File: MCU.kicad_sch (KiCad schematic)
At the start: 28 parts, among them U2 STM32H743VIT6, Y1 8MHz

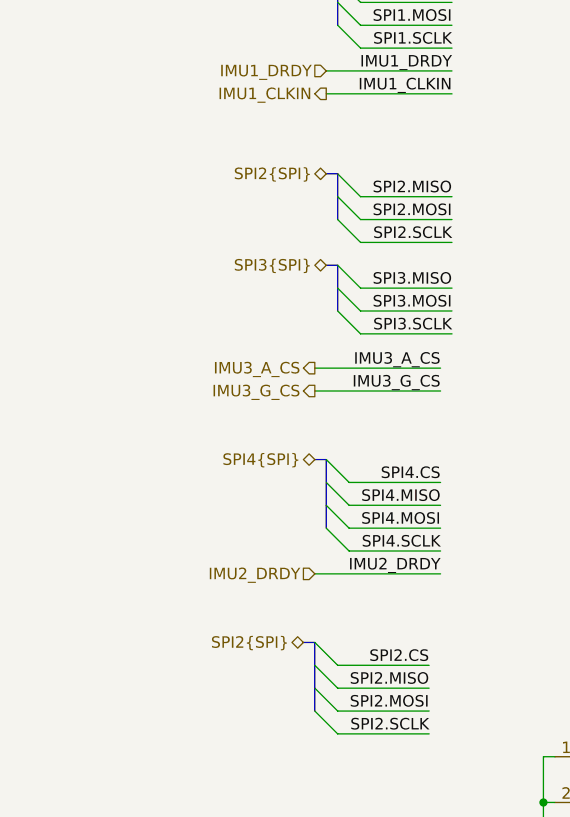
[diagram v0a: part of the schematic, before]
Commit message: Define SPI2 bus members across MCU and sensors
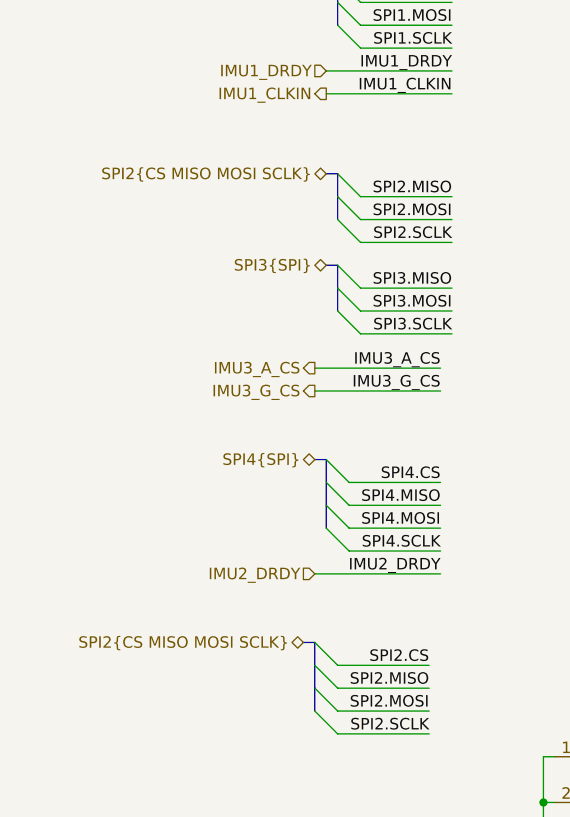
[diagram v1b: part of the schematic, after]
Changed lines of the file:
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@@
 		)
 	)
-	(hierarchical_label "SPI2{SPI}"
+	(hierarchical_label "SPI2{CS MISO MOSI SCLK}"
 		(shape bidirectional)
 		(at 30.48 130.81 180)
@@
 		)
 	)
-	(hierarchical_label "SPI2{SPI}"
+	(hierarchical_label "SPI2{CS MISO MOSI SCLK}"
 		(shape bidirectional)
 		(at 33.02 78.74 180)

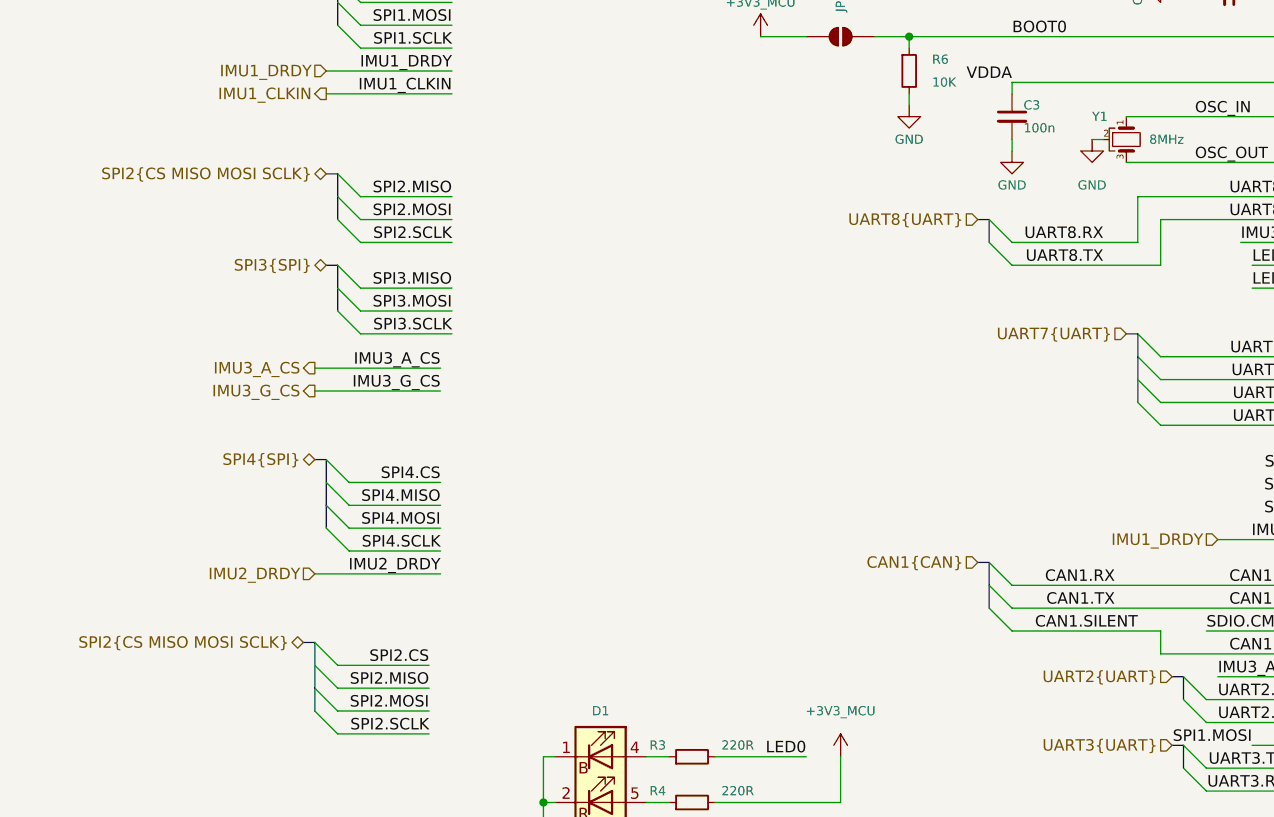
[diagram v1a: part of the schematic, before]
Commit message: Define reusable aliases for hierarchical buses
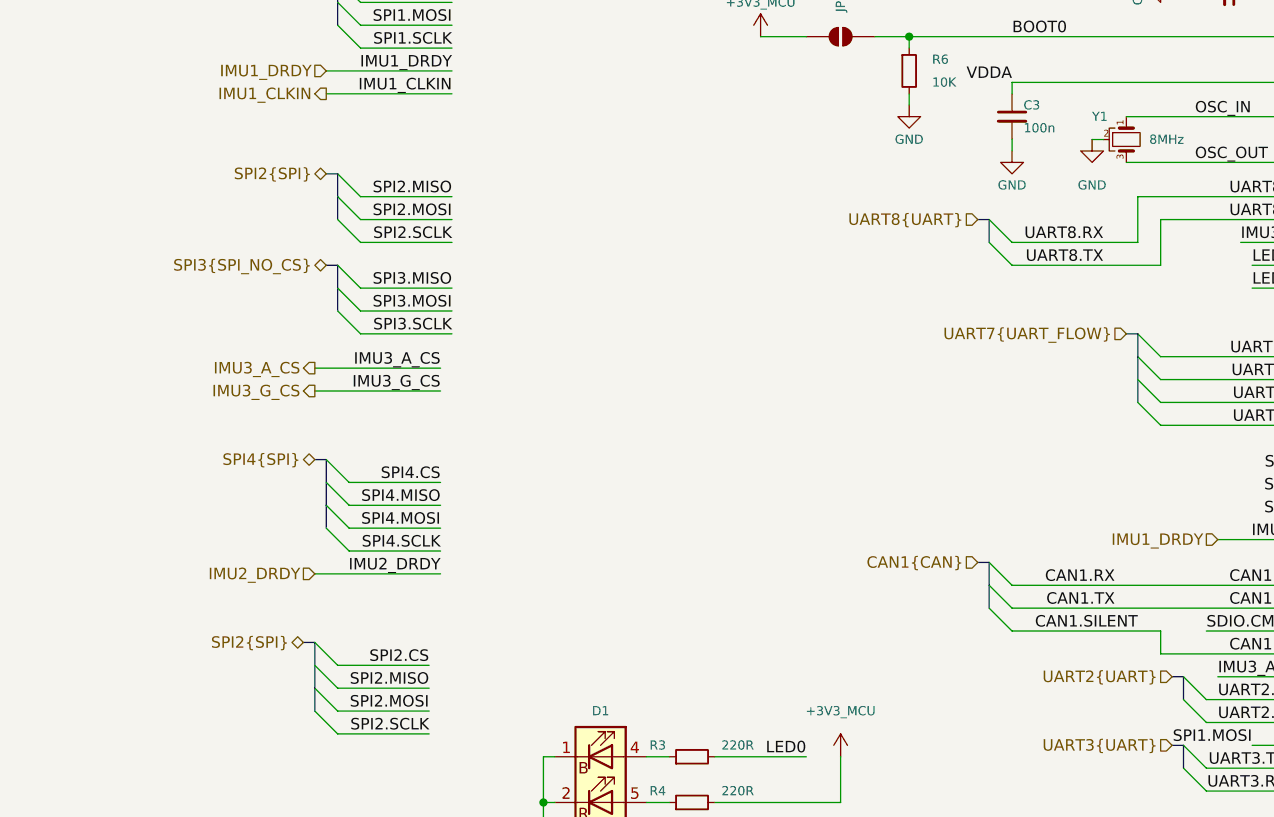
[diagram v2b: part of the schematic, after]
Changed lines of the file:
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@@
 		)
 	)
-	(hierarchical_label "SPI3{SPI}"
+	(hierarchical_label "SPI3{SPI_NO_CS}"
 		(shape bidirectional)
 		(at 33.02 88.9 180)
@@
 		)
 	)
-	(hierarchical_label "SPI2{CS MISO MOSI SCLK}"
+	(hierarchical_label "SPI2{SPI}"
 		(shape bidirectional)
 		(at 30.48 130.81 180)
@@
 		)
 	)
-	(hierarchical_label "SPI2{CS MISO MOSI SCLK}"
+	(hierarchical_label "SPI2{SPI}"
 		(shape bidirectional)
 		(at 33.02 78.74 180)
@@
 		)
 	)
-	(hierarchical_label "UART7{UART}"
+	(hierarchical_label "UART7{UART_FLOW}"
 		(shape input)
 		(at 121.92 96.52 180)

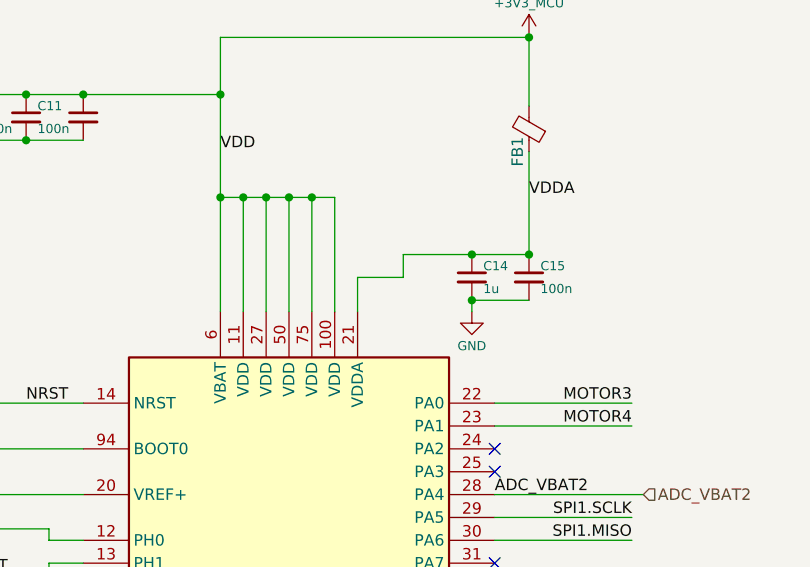
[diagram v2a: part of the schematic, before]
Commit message: Declare external and regulator power sources for ERC
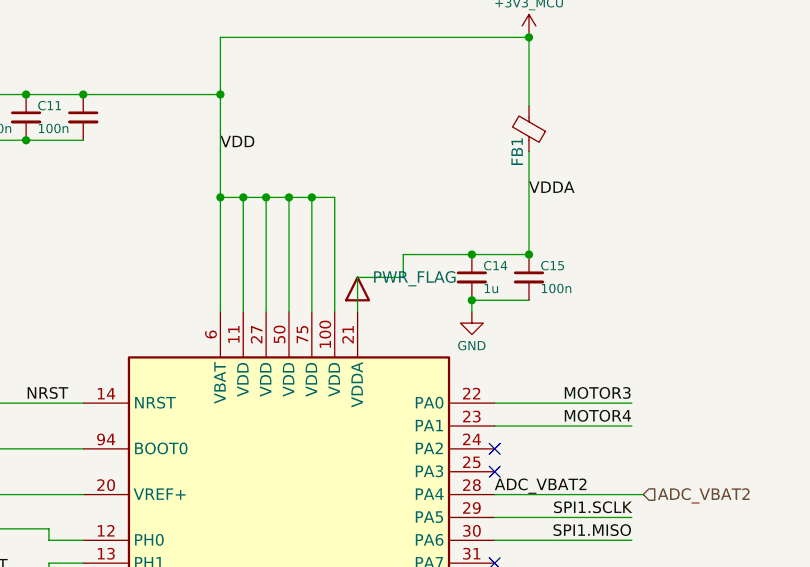
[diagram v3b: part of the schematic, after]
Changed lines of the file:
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@@
 		)
 	)
+	(symbol
+    (lib_id "FC01_Project:ERC__POWER_SOURCE") (at 176.53 48.26 0) (unit 1)
+    (exclude_from_sim no) (in_bom no) (on_board no) (dnp no)
+    (property "Reference" "#FLG201" (at 176.53 52.07 0) (hide yes) (effects (font (size 1.27 1.27))))
+    (property "Value" "PWR_FLAG" (at 182.88 44.45 0) (effects (font (size 1.27 1.27))))
+    (pin "1")
+    (instances (project "H743_Ardupilot" (path "/6b768b36-fce6-4be0-9021-6d41bddc3a70/020f93d0-ab76-4c08-9373-958d923a454f" (reference "#FLG201") (unit 1)))))
 )

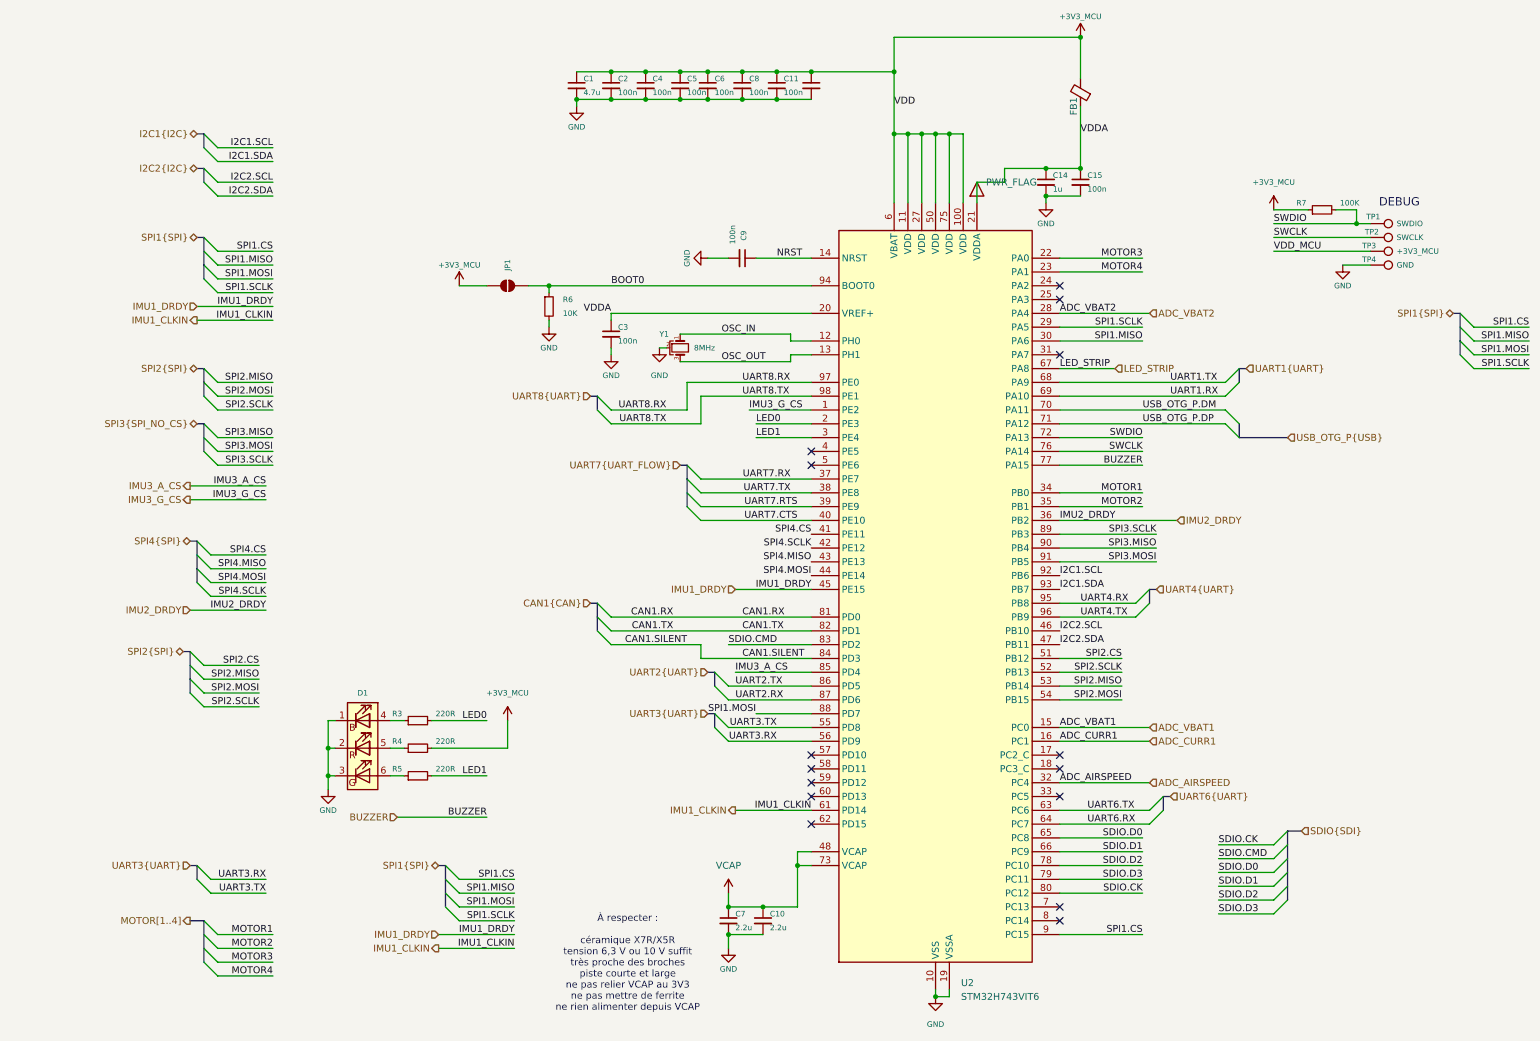
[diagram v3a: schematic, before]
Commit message: Correct ERC pin models and power connectivity
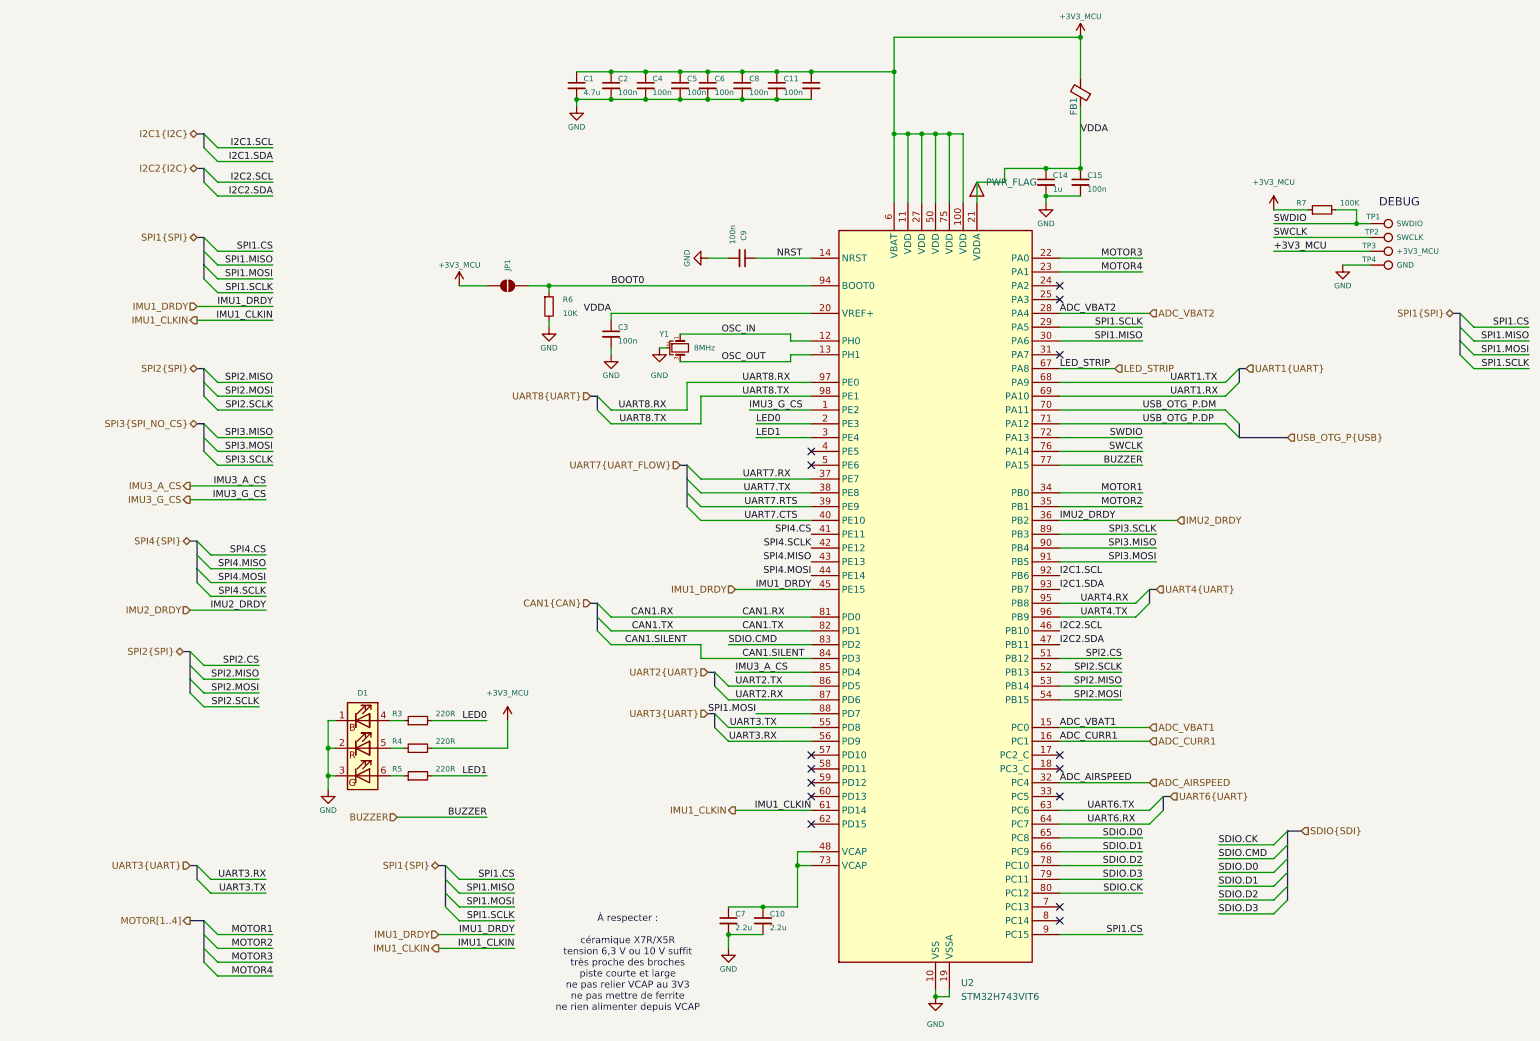
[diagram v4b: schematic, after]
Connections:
- net VDD_MCU is gone; now on net +3V3_MCU: TP3.1
- net VCAP: no longer names the net of C10.1, C7.1, U2.48 (VCAP), U2.73 (VCAP)
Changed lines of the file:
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@@
 	)
 	(junction
-		(at 130.81 177.8)
-		(diameter 0)
-		(color 0 0 0 0)
-	)
-	(junction
 		(at 109.22 29.21)
 		(diameter 0)
@@
 		)
 	)
-	(wire
-		(pts
-			(xy 130.81 175.26) (xy 130.81 177.8)
-		)
-		(stroke
-			(width 0)
-			(type default)
-		)
-	)
 	(bus
 		(pts
@@
 	(wire
 		(pts
-			(xy 130.81 177.8) (xy 137.16 177.8)
-		)
-		(stroke
-			(width 0)
-			(type default)
-		)
-	)
-	(wire
-		(pts
 			(xy 168.91 194.31) (xy 168.91 193.04)
 		)
@@
 		)
 	)
-	(label "VDD_MCU"
+	(label "+3V3_MCU"
 		(at 231.14 57.15 0)
 		(effects
@@
 		)
 	)
-	(label "VDD"
-		(at 161.29 30.48 0)
-		(effects
-			(font
-				(size 1.27 1.27)
-			)
-			(justify left bottom)
-		)
-	)
 	(label "I2C2.SDA"
 		(at 191.77 129.54 0)
@@
 	)
 	(symbol
-		(lib_id "FC01_Project:MCU__VDD")
-		(at 130.81 175.26 0)
-		(unit 1)
-		(body_style 1)
-		(exclude_from_sim no)
-		(in_bom yes)
-		(on_board yes)
-		(in_pos_files yes)
-		(dnp no)
-		(fields_autoplaced yes)
-		(property "Reference" "#PWR017"
-			(at 130.81 179.07 0)
-			(hide yes)
-			(show_name no)
-			(do_not_autoplace no)
-			(effects
-				(font
-					(size 1.27 1.27)
-				)
-			)
-		)
-		(property "Value" "VCAP"
-			(at 130.81 170.18 0)
-			(show_name no)
-			(do_not_autoplace no)
-			(effects
-				(font
-					(size 1.27 1.27)
-				)
-			)
-		)
-		(property "Footprint" ""
-			(at 130.81 175.26 0)
-			(hide yes)
-			(show_name no)
-			(do_not_autoplace no)
-			(effects
-				(font
-					(size 1.27 1.27)
-				)
-			)
-		)
-		(property "Datasheet" ""
-			(at 130.81 175.26 0)
-			(hide yes)
-			(show_name no)
-			(do_not_autoplace no)
-			(effects
-				(font
-					(size 1.27 1.27)
-				)
-			)
-		)
-		(property "Description" "Power symbol creates a global label with name \"VDD\""
-			(at 130.81 175.26 0)
-			(hide yes)
-			(show_name no)
-			(do_not_autoplace no)
-			(effects
-				(font
-					(size 1.27 1.27)
-				)
-			)
-		)
-		(pin "1"
-		)
-		(instances
-			(project "H743_Ardupilot"
-				(path "/6b768b36-fce6-4be0-9021-6d41bddc3a70/020f93d0-ab76-4c08-9373-958d923a454f"
-					(reference "#PWR017")
-					(unit 1)
-				)
-			)
-			(project "MCU"
-				(path "/dac36f26-6ddd-4279-ab20-a26c5ba5f958"
-					(reference "#PWR017")
-					(unit 1)
-				)
-			)
-		)
-	)
-	(symbol
 		(lib_id "FC01_Project:MCU__C_Small")
 		(at 102.87 26.67 0)
@@
     (pin "1")
     (instances (project "H743_Ardupilot" (path "/6b768b36-fce6-4be0-9021-6d41bddc3a70/020f93d0-ab76-4c08-9373-958d923a454f" (reference "#FLG201") (unit 1)))))
+	(wire (pts (xy 130.81 177.8) (xy 137.16 177.8)) (stroke (width 0) (type default)))
 )
